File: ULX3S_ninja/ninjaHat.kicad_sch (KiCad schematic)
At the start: 33 parts, among them J1 DVI-HX-107DIP, P1 ULX3S connector (JP1)

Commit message: Schematic fix
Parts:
- removed TP1, TP10, TP11, TP14, TP16, TP2, TP3, TP4, TP5, TP6, TP7, TP8: TestPoint, TestPoint:TestPoint_Pad_D1.5mm, symbol Connector:TestPoint
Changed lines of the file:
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@@
     (pin "2")
-  )
-  (symbol (lib_id "Connector:TestPoint") (at 137.16 113.03 270) (unit 1)
-    (in_bom yes) (on_board yes)
-    (property "Reference" "TP6" (id 0) (at 153.67 113.03 90))
-    (property "Value" "TestPoint" (id 1) (at 146.05 113.03 90))
-    (property "Footprint" "TestPoint:TestPoint_Pad_D1.5mm" (id 2) (at 137.16 118.11 0)
-      (effects (font (size 1.27 1.27)) hide)
-    )
-    (property "Datasheet" "~" (id 3) (at 137.16 118.11 0)
-      (effects (font (size 1.27 1.27)) hide)
-    )
-    (pin "1")
   )
   (symbol (lib_id "Device:R") (at 82.55 55.88 90) (unit 1)
@@
     (pin "2")
   )
-  (symbol (lib_id "Connector:TestPoint") (at 137.16 110.49 270) (unit 1)
-    (in_bom yes) (on_board yes)
-    (property "Reference" "TP5" (id 0) (at 153.67 110.49 90))
-    (property "Value" "TestPoint" (id 1) (at 146.05 110.49 90))
-    (property "Footprint" "TestPoint:TestPoint_Pad_D1.5mm" (id 2) (at 137.16 115.57 0)
-      (effects (font (size 1.27 1.27)) hide)
-    )
-    (property "Datasheet" "~" (id 3) (at 137.16 115.57 0)
-      (effects (font (size 1.27 1.27)) hide)
-    )
-    (pin "1")
-  )
   (symbol (lib_id "Device:R") (at 140.97 48.26 90) (unit 1)
     (in_bom yes) (on_board yes)
@@
     (pin "1")
   )
-  (symbol (lib_id "Connector:TestPoint") (at 88.265 120.65 90) (unit 1)
-    (in_bom yes) (on_board yes)
-    (property "Reference" "TP7" (id 0) (at 71.755 120.65 90))
-    (property "Value" "TestPoint" (id 1) (at 79.375 120.65 90))
-    (property "Footprint" "TestPoint:TestPoint_Pad_D1.5mm" (id 2) (at 88.265 115.57 0)
-      (effects (font (size 1.27 1.27)) hide)
-    )
-    (property "Datasheet" "~" (id 3) (at 88.265 115.57 0)
-      (effects (font (size 1.27 1.27)) hide)
-    )
-    (pin "1")
-  )
   (symbol (lib_id "Device:R") (at 140.97 66.04 90) (unit 1)
     (in_bom yes) (on_board yes)
@@
     (pin "2")
   )
-  (symbol (lib_id "Connector:TestPoint") (at 137.16 105.41 270) (unit 1)
-    (in_bom yes) (on_board yes)
-    (property "Reference" "TP2" (id 0) (at 153.67 105.41 90))
-    (property "Value" "TestPoint" (id 1) (at 146.05 105.41 90))
-    (property "Footprint" "TestPoint:TestPoint_Pad_D1.5mm" (id 2) (at 137.16 110.49 0)
-      (effects (font (size 1.27 1.27)) hide)
-    )
-    (property "Datasheet" "~" (id 3) (at 137.16 110.49 0)
-      (effects (font (size 1.27 1.27)) hide)
-    )
-    (pin "1")
-  )
   (symbol (lib_id "Connector:TestPoint") (at 137.16 148.59 270) (unit 1)
     (in_bom yes) (on_board yes)
@@
     (pin "1")
   )
-  (symbol (lib_id "Connector:TestPoint") (at 88.265 125.73 90) (unit 1)
-    (in_bom yes) (on_board yes)
-    (property "Reference" "TP10" (id 0) (at 71.755 125.73 90))
-    (property "Value" "TestPoint" (id 1) (at 79.375 125.73 90))
-    (property "Footprint" "TestPoint:TestPoint_Pad_D1.5mm" (id 2) (at 88.265 120.65 0)
-      (effects (font (size 1.27 1.27)) hide)
-    )
-    (property "Datasheet" "~" (id 3) (at 88.265 120.65 0)
-      (effects (font (size 1.27 1.27)) hide)
-    )
-    (pin "1")
-  )
   (symbol (lib_id "Device:R") (at 140.97 50.8 90) (unit 1)
     (in_bom yes) (on_board yes)
@@
     (pin "1")
   )
-  (symbol (lib_id "Connector:TestPoint") (at 88.265 135.89 90) (unit 1)
-    (in_bom yes) (on_board yes)
-    (property "Reference" "TP14" (id 0) (at 71.755 135.89 90))
-    (property "Value" "TestPoint" (id 1) (at 79.375 135.89 90))
-    (property "Footprint" "TestPoint:TestPoint_Pad_D1.5mm" (id 2) (at 88.265 130.81 0)
-      (effects (font (size 1.27 1.27)) hide)
-    )
-    (property "Datasheet" "~" (id 3) (at 88.265 130.81 0)
-      (effects (font (size 1.27 1.27)) hide)
-    )
-    (pin "1")
-  )
   (symbol (lib_id "power:GND") (at 137.16 148.59 270) (mirror x) (unit 1)
     (in_bom yes) (on_board yes)
@@
     (pin "2")
   )
-  (symbol (lib_id "Connector:TestPoint") (at 137.16 125.73 270) (unit 1)
-    (in_bom yes) (on_board yes)
-    (property "Reference" "TP11" (id 0) (at 153.67 125.73 90))
-    (property "Value" "TestPoint" (id 1) (at 146.05 125.73 90))
-    (property "Footprint" "TestPoint:TestPoint_Pad_D1.5mm" (id 2) (at 137.16 130.81 0)
-      (effects (font (size 1.27 1.27)) hide)
-    )
-    (property "Datasheet" "~" (id 3) (at 137.16 130.81 0)
-      (effects (font (size 1.27 1.27)) hide)
-    )
-    (pin "1")
-  )
-  (symbol (lib_id "Connector:TestPoint") (at 88.265 140.97 90) (unit 1)
-    (in_bom yes) (on_board yes)
-    (property "Reference" "TP16" (id 0) (at 71.755 140.97 90))
-    (property "Value" "TestPoint" (id 1) (at 79.375 140.97 90))
-    (property "Footprint" "TestPoint:TestPoint_Pad_D1.5mm" (id 2) (at 88.265 135.89 0)
-      (effects (font (size 1.27 1.27)) hide)
-    )
-    (property "Datasheet" "~" (id 3) (at 88.265 135.89 0)
-      (effects (font (size 1.27 1.27)) hide)
-    )
-    (pin "1")
-  )
-  (symbol (lib_id "Connector:TestPoint") (at 88.265 105.41 90) (unit 1)
-    (in_bom yes) (on_board yes)
-    (property "Reference" "TP1" (id 0) (at 71.755 105.41 90))
-    (property "Value" "TestPoint" (id 1) (at 79.375 105.41 90))
-    (property "Footprint" "TestPoint:TestPoint_Pad_D1.5mm" (id 2) (at 88.265 100.33 0)
-      (effects (font (size 1.27 1.27)) hide)
-    )
-    (property "Datasheet" "~" (id 3) (at 88.265 100.33 0)
-      (effects (font (size 1.27 1.27)) hide)
-    )
-    (pin "1")
-  )
   (symbol (lib_id "power:+3V3") (at 137.16 152.4 90) (unit 1)
     (in_bom yes) (on_board yes)
@@
     )
     (property "Datasheet" "" (id 3) (at 137.16 152.4 0)
-      (effects (font (size 1.27 1.27)) hide)
-    )
-    (pin "1")
-  )
-  (symbol (lib_id "Connector:TestPoint") (at 137.16 120.65 270) (unit 1)
-    (in_bom yes) (on_board yes)
-    (property "Reference" "TP8" (id 0) (at 153.67 120.65 90))
-    (property "Value" "TestPoint" (id 1) (at 146.05 120.65 90))
-    (property "Footprint" "TestPoint:TestPoint_Pad_D1.5mm" (id 2) (at 137.16 125.73 0)
-      (effects (font (size 1.27 1.27)) hide)
-    )
-    (property "Datasheet" "~" (id 3) (at 137.16 125.73 0)
       (effects (font (size 1.27 1.27)) hide)
     )
@@
     (pin "1")
   )
-  (symbol (lib_id "Connector:TestPoint") (at 88.265 110.49 90) (unit 1)
-    (in_bom yes) (on_board yes)
-    (property "Reference" "TP4" (id 0) (at 71.755 110.49 90))
-    (property "Value" "TestPoint" (id 1) (at 79.375 110.49 90))
-    (property "Footprint" "TestPoint:TestPoint_Pad_D1.5mm" (id 2) (at 88.265 105.41 0)
-      (effects (font (size 1.27 1.27)) hide)
-    )
-    (property "Datasheet" "~" (id 3) (at 88.265 105.41 0)
-      (effects (font (size 1.27 1.27)) hide)
-    )
-    (pin "1")
-  )
   (symbol (lib_id "power:GND") (at 119.38 83.82 90) (unit 1)
     (in_bom yes) (on_board yes)
@@
     (property "Footprint" "" (id 2) (at 119.38 83.82 0))
     (property "Datasheet" "" (id 3) (at 119.38 83.82 0))
-    (pin "1")
-  )
-  (symbol (lib_id "Connector:TestPoint") (at 137.16 107.95 270) (unit 1)
-    (in_bom yes) (on_board yes)
-    (property "Reference" "TP3" (id 0) (at 153.67 107.95 90))
-    (property "Value" "TestPoint" (id 1) (at 146.05 107.95 90))
-    (property "Footprint" "TestPoint:TestPoint_Pad_D1.5mm" (id 2) (at 137.16 113.03 0)
-      (effects (font (size 1.27 1.27)) hide)
-    )
-    (property "Datasheet" "~" (id 3) (at 137.16 113.03 0)
-      (effects (font (size 1.27 1.27)) hide)
-    )
     (pin "1")
   )
@@
       (reference "R12") (unit 1) (value "50R") (footprint "Resistor_SMD:R_0805_2012Metric")
     )
-    (path "/a1d24376-61a3-442c-8eec-0ad10b6ec49a"
-      (reference "TP1") (unit 1) (value "TestPoint") (footprint "TestPoint:TestPoint_Pad_D1.5mm")
-    )
-    (path "/425f478e-b626-4aac-802e-83a504ac26ca"
-      (reference "TP2") (unit 1) (value "TestPoint") (footprint "TestPoint:TestPoint_Pad_D1.5mm")
-    )
-    (path "/b48a059e-b178-4079-870c-e42a98b7ca64"
-      (reference "TP3") (unit 1) (value "TestPoint") (footprint "TestPoint:TestPoint_Pad_D1.5mm")
-    )
-    (path "/adc24f8d-a076-40d3-baae-d9f4a04d3da7"
-      (reference "TP4") (unit 1) (value "TestPoint") (footprint "TestPoint:TestPoint_Pad_D1.5mm")
-    )
-    (path "/0cbcf4ed-9354-488d-b02d-a05b4d76e139"
-      (reference "TP5") (unit 1) (value "TestPoint") (footprint "TestPoint:TestPoint_Pad_D1.5mm")
-    )
-    (path "/02906bdc-870a-4740-81bb-4efe5e4db61e"
-      (reference "TP6") (unit 1) (value "TestPoint") (footprint "TestPoint:TestPoint_Pad_D1.5mm")
-    )
-    (path "/3198817b-6f67-4f3c-aed8-4dc269dff70f"
-      (reference "TP7") (unit 1) (value "TestPoint") (footprint "TestPoint:TestPoint_Pad_D1.5mm")
-    )
-    (path "/a2d7fff1-a08c-493f-b75a-57c4b86aecc0"
-      (reference "TP8") (unit 1) (value "TestPoint") (footprint "TestPoint:TestPoint_Pad_D1.5mm")
-    )
     (path "/62ad9929-ec78-41af-967c-c86841fc209c"
       (reference "TP9") (unit 1) (value "TestPoint") (footprint "TestPoint:TestPoint_Pad_D1.5mm")
     )
-    (path "/6793b199-fe12-4a16-aa32-0c74f6dfe7fe"
-      (reference "TP10") (unit 1) (value "TestPoint") (footprint "TestPoint:TestPoint_Pad_D1.5mm")
-    )
-    (path "/96cf87b1-2e43-4368-a8d1-c7f2e52bc9de"
-      (reference "TP11") (unit 1) (value "TestPoint") (footprint "TestPoint:TestPoint_Pad_D1.5mm")
-    )
     (path "/fc8bf555-146f-4907-8930-e657650add49"
       (reference "TP12") (unit 1) (value "TestPoint") (footprint "TestPoint:TestPoint_Pad_D1.5mm")
@@
       (reference "TP13") (unit 1) (value "TestPoint") (footprint "TestPoint:TestPoint_Pad_D1.5mm")
     )
-    (path "/827b95ad-a91d-4c7c-bf8e-e1cfc4b64370"
-      (reference "TP14") (unit 1) (value "TestPoint") (footprint "TestPoint:TestPoint_Pad_D1.5mm")
-    )
     (path "/a3de2bad-f7fe-4753-9194-4870bbad05b2"
       (reference "TP15") (unit 1) (value "TestPoint") (footprint "TestPoint:TestPoint_Pad_D1.5mm")
     )
-    (path "/9eec8b79-c070-4ba7-bc99-43a3f0478870"
-      (reference "TP16") (unit 1) (value "TestPoint") (footprint "TestPoint:TestPoint_Pad_D1.5mm")
-    )
     (path "/20b3079c-6fa5-4d5d-b1e0-4366244760b4"

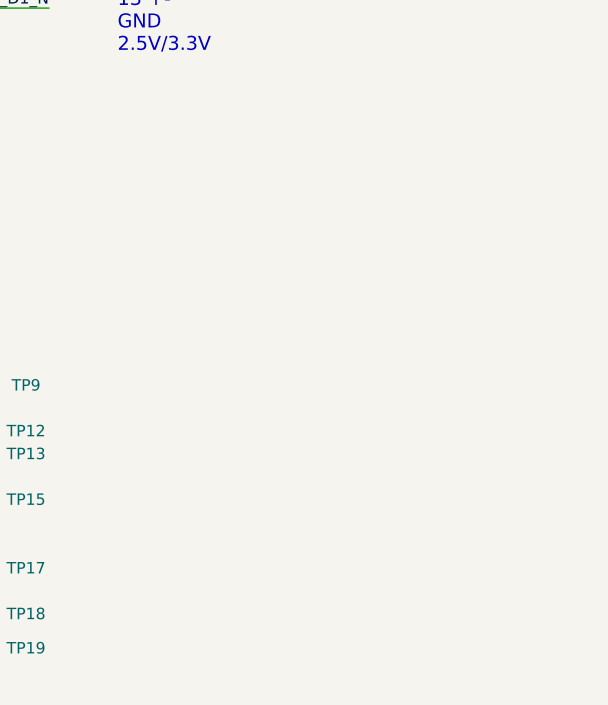
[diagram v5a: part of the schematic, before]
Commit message: added pinheaders for D0 D1 and CLK (cam0 only) for debugging
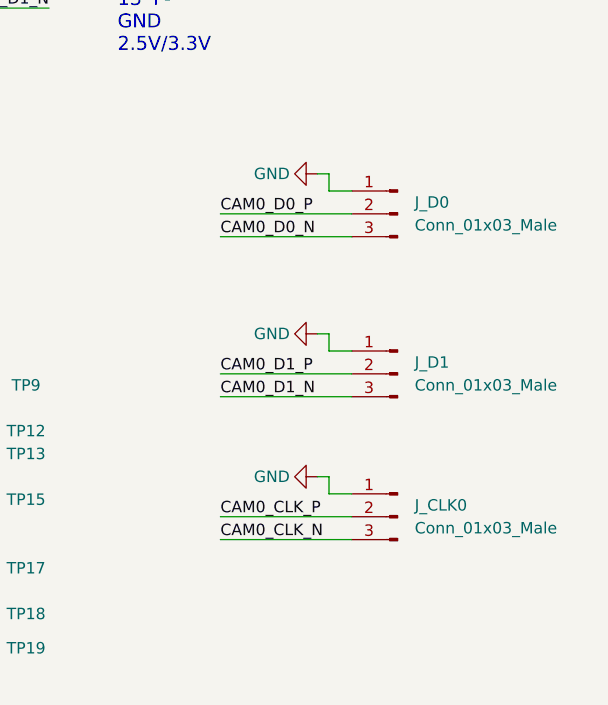
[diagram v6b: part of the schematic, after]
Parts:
- added J_CLK0, J_D0, J_D1: Conn_01x03_Male, Connector_PinHeader_1.27mm:PinHeader_1x03_P1.27mm_Vertical, symbol Connector:Conn_01x03_Male
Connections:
- net CAM0_CLK_N: now also J_CLK0.3 (Pin_3)
- net CAM0_CLK_P: now also J_CLK0.2 (Pin_2)
- net CAM0_D0_N: now also J_D0.3 (Pin_3)
- net CAM0_D0_P: now also J_D0.2 (Pin_2)
- net CAM0_D1_N: now also J_D1.3 (Pin_3)
- net CAM0_D1_P: now also J_D1.2 (Pin_2)
- net GND: now also J_CLK0.1 (Pin_1), J_D0.1 (Pin_1), J_D1.1 (Pin_1)

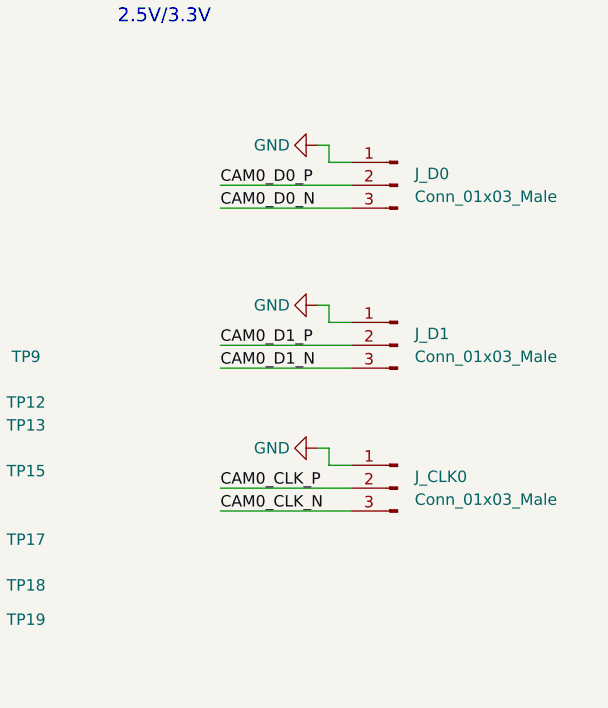
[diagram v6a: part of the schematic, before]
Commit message: added 2nd gnd pin to debugging connectors
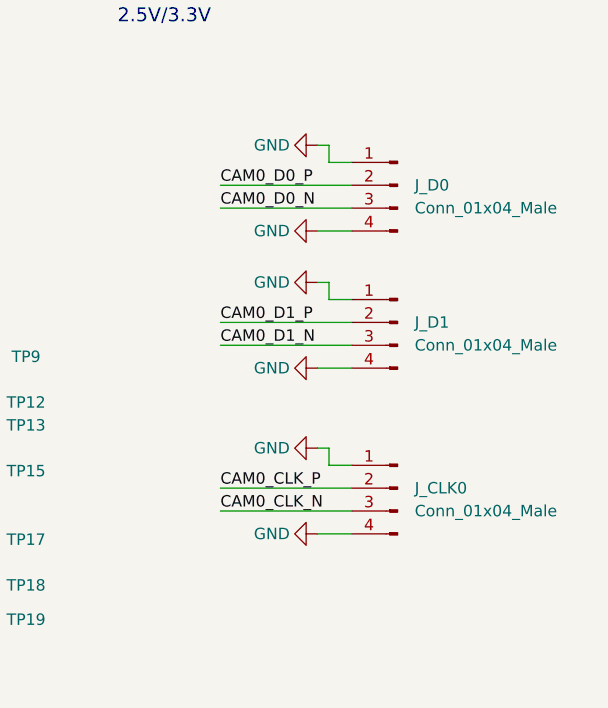
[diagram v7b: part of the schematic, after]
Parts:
- removed J_CLK0, J_D0, J_D1: Conn_01x03_Male, Connector_PinHeader_1.27mm:PinHeader_1x03_P1.27mm_Vertical, symbol Connector:Conn_01x03_Male
- added J_CLK0, J_D0, J_D1: Conn_01x04_Male, Connector_PinHeader_1.27mm:PinHeader_1x04_P1.27mm_Vertical, symbol Connector:Conn_01x04_Male
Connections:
- net CAM0_CLK_N: now also J_CLK0.3 (Pin_3)
- net CAM0_CLK_P: now also J_CLK0.2 (Pin_2)
- net CAM0_D0_N: now also J_D0.3 (Pin_3)
- net CAM0_D0_P: now also J_D0.2 (Pin_2)
- net CAM0_D1_N: now also J_D1.3 (Pin_3)
- net CAM0_D1_P: now also J_D1.2 (Pin_2)
- net GND: now also J_CLK0.1 (Pin_1), J_CLK0.4 (Pin_4), J_D0.1 (Pin_1), J_D0.4 (Pin_4), J_D1.1 (Pin_1), J_D1.4 (Pin_4)

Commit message: fixed pin header footprint
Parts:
- J_CLK0, J_D0, J_D1: footprint Connector_PinHeader_1.27mm:PinHeader_1x04_P1.27mm_Vertical -> Connector_PinHeader_2.54mm:PinHeader_1x04_P2.54mm_Vertical
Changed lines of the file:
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@@
       (effects (font (size 1.27 1.27)) (justify right))
     )
-    (property "Footprint" "Connector_PinHeader_1.27mm:PinHeader_1x04_P1.27mm_Vertical" (id 2) (at 194.945 137.795 0)
+    (property "Footprint" "Connector_PinHeader_2.54mm:PinHeader_1x04_P2.54mm_Vertical" (id 2) (at 194.945 137.795 0)
       (effects (font (size 1.27 1.27)) hide)
     )
@@
       (effects (font (size 1.27 1.27)) (justify right))
     )
-    (property "Footprint" "Connector_PinHeader_1.27mm:PinHeader_1x04_P1.27mm_Vertical" (id 2) (at 194.945 104.14 0)
+    (property "Footprint" "Connector_PinHeader_2.54mm:PinHeader_1x04_P2.54mm_Vertical" (id 2) (at 194.945 104.14 0)
       (effects (font (size 1.27 1.27)) hide)
     )
@@
       (effects (font (size 1.27 1.27)) (justify right))
     )
-    (property "Footprint" "Connector_PinHeader_1.27mm:PinHeader_1x04_P1.27mm_Vertical" (id 2) (at 194.945 119.38 0)
+    (property "Footprint" "Connector_PinHeader_2.54mm:PinHeader_1x04_P2.54mm_Vertical" (id 2) (at 194.945 119.38 0)
       (effects (font (size 1.27 1.27)) hide)
     )
@@
     )
     (path "/48f8d505-a115-4149-8d3c-b4e46f8d3625"
-      (reference "J_CLK0") (unit 1) (value "Conn_01x04_Male") (footprint "Connector_PinHeader_1.27mm:PinHeader_1x04_P1.27mm_Vertical")
+      (reference "J_CLK0") (unit 1) (value "Conn_01x04_Male") (footprint "Connector_PinHeader_2.54mm:PinHeader_1x04_P2.54mm_Vertical")
     )
     (path "/aca7442c-5526-4642-be31-874350a33514"
-      (reference "J_D0") (unit 1) (value "Conn_01x04_Male") (footprint "Connector_PinHeader_1.27mm:PinHeader_1x04_P1.27mm_Vertical")
+      (reference "J_D0") (unit 1) (value "Conn_01x04_Male") (footprint "Connector_PinHeader_2.54mm:PinHeader_1x04_P2.54mm_Vertical")
     )
     (path "/d425c7cc-30c2-47b6-9531-9feded17be55"
-      (reference "J_D1") (unit 1) (value "Conn_01x04_Male") (footprint "Connector_PinHeader_1.27mm:PinHeader_1x04_P1.27mm_Vertical")
+      (reference "J_D1") (unit 1) (value "Conn_01x04_Male") (footprint "Connector_PinHeader_2.54mm:PinHeader_1x04_P2.54mm_Vertical")
     )
     (path "/00000000-0000-0000-0000-000059ad464a"
